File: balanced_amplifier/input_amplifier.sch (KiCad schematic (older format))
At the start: 47 parts, among them U1 LM4562, U2 LM4562, U3 NE5532, U4 LM4562

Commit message: specify resistor details
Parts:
- R1, R13, R16, R4: Distributor (none) -> Digikey; Distributor PN (none) -> YAG2320CT-ND; Manufacturer (none) -> Yageo; Manufacturer PN (none) -> RT0603FRE07100RL; URL (none) -> https://www.digikey.com/product-detail/en/yageo/RT0603FRE07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; Unit Price (none) -> 0.10
- R10, R11, R19, R20, R22, R23, R7, R8: Distributor (none) -> Digikey; Distributor PN (none) -> P820DBCT-ND; Manufacturer (none) -> Panasonic; Manufacturer PN (none) -> ERA-3AEB821V; URL (none) -> https://www.digikey.com/product-detail/en/panasonic-electro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; Unit Price (none) -> 0.35
- R12, R21, R24, R9: Distributor (none) -> Digikey; Distributor PN (none) -> P1.6KBCCT-ND; Manufacturer (none) -> Panasonic; Manufacturer PN (none) -> ERA-8AEB162V; URL (none) -> https://www.digikey.com/product-detail/en/panasonic-electro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; Unit Price (none) -> 0.66
- R14, R15, R17, R18, R2, R3, R5, R6: Distributor (none) -> Digikey; Distributor PN (none) -> 311-2103-1-ND; Manufacturer (none) -> Yageo; Manufacturer PN (none) -> AT0603DRD07100KL; URL (none) -> https://www.digikey.com/product-detail/en/yageo/AT0603DRD07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; Unit Price (none) -> 0.25

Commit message: Assign footprint to potentiometers
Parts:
- RV1: footprint (none) -> Potentiometer_THT_custom:Potentiometer_Bourns_91_Dual_Horizontal
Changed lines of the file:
@@
 F 0 "RV1" H 8430 1246 50  0000 R CNN
 F 1 "5k" H 8430 1155 50  0000 R CNN
-F 2 "" H 8500 1200 50  0001 C CNN
+F 2 "Potentiometer_THT_custom:Potentiometer_Bourns_91_Dual_Horizontal" H 8500 1200 50  0001 C CNN
 F 3 "https://www.bourns.com/docs/Product-Datasheets/91_95.pdf" H 8500 1200 50  0001 C CNN
 F 4 "Bourns" H 8500 1200 50  0001 C CNN "Manufacturer"
@@
 F 0 "RV1" H 8431 4254 50  0000 R CNN
 F 1 "5k" H 8431 4345 50  0000 R CNN
-F 2 "" H 8500 4300 50  0001 C CNN
+F 2 "Potentiometer_THT_custom:Potentiometer_Bourns_91_Dual_Horizontal" H 8500 4300 50  0001 C CNN
 F 3 "https://www.bourns.com/docs/Product-Datasheets/91_95.pdf" H 8500 4300 50  0001 C CNN
 F 4 "Bourns" H 8500 4300 50  0001 C CNN "Manufacturer"

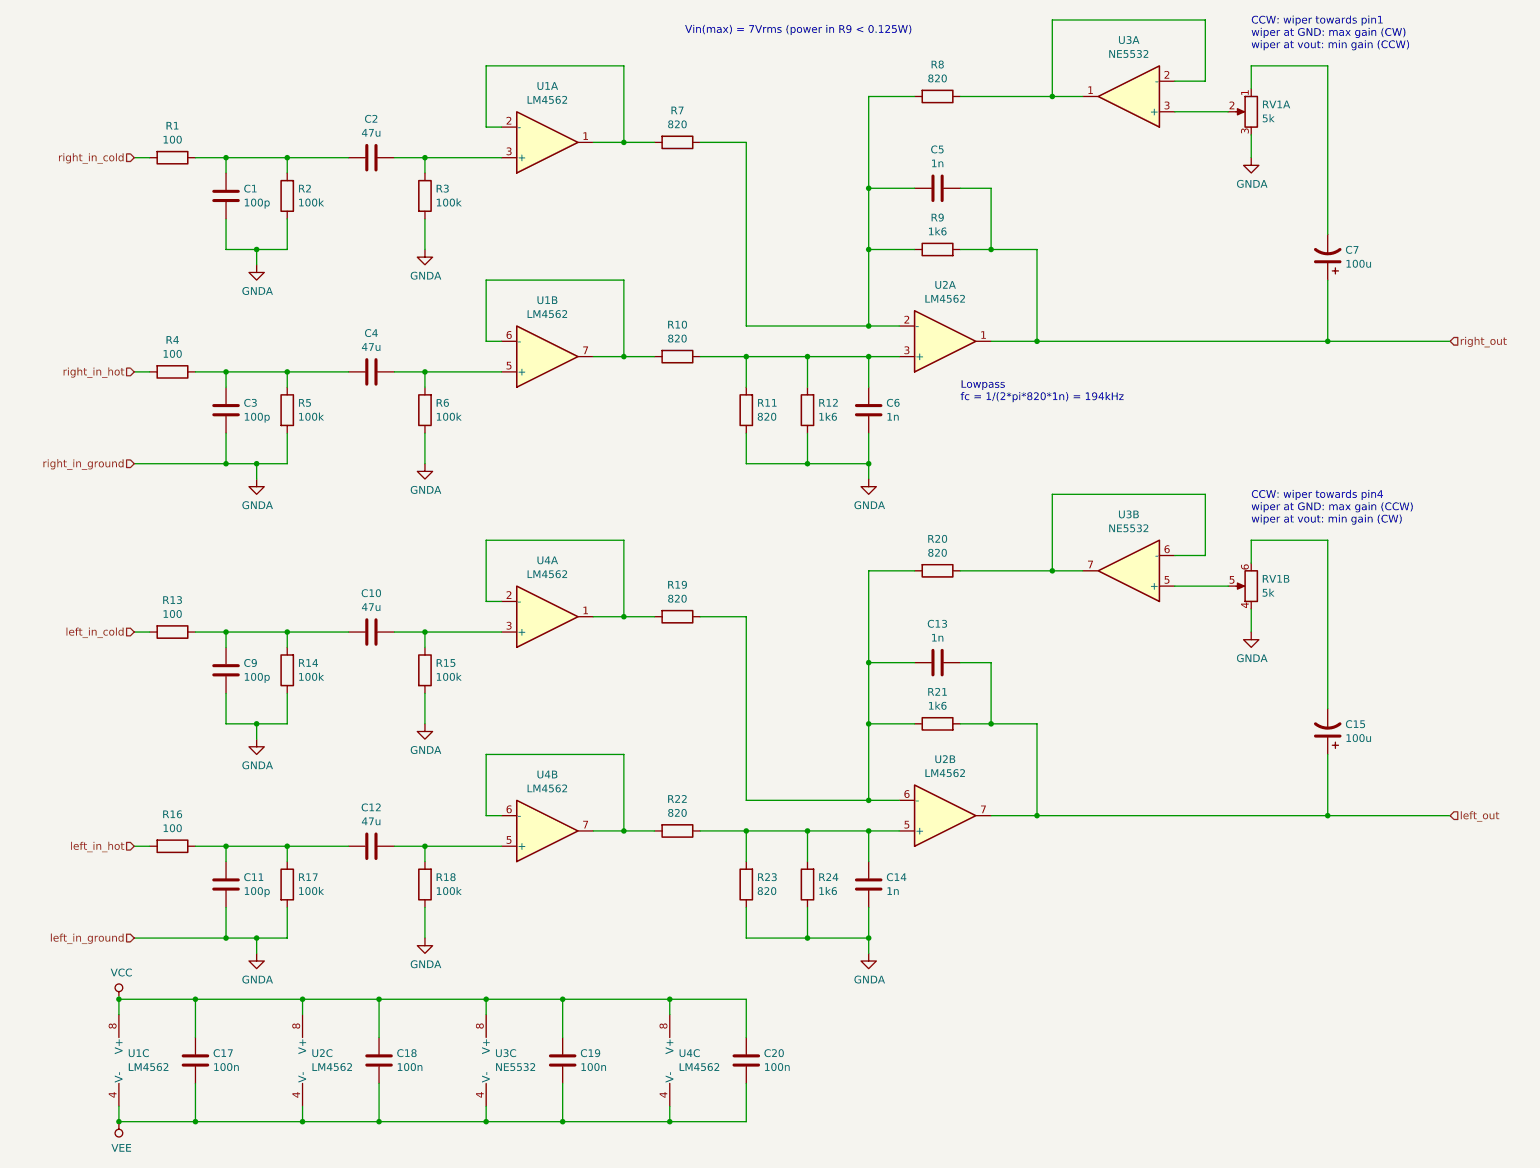
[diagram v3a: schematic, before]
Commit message: Add testpoints
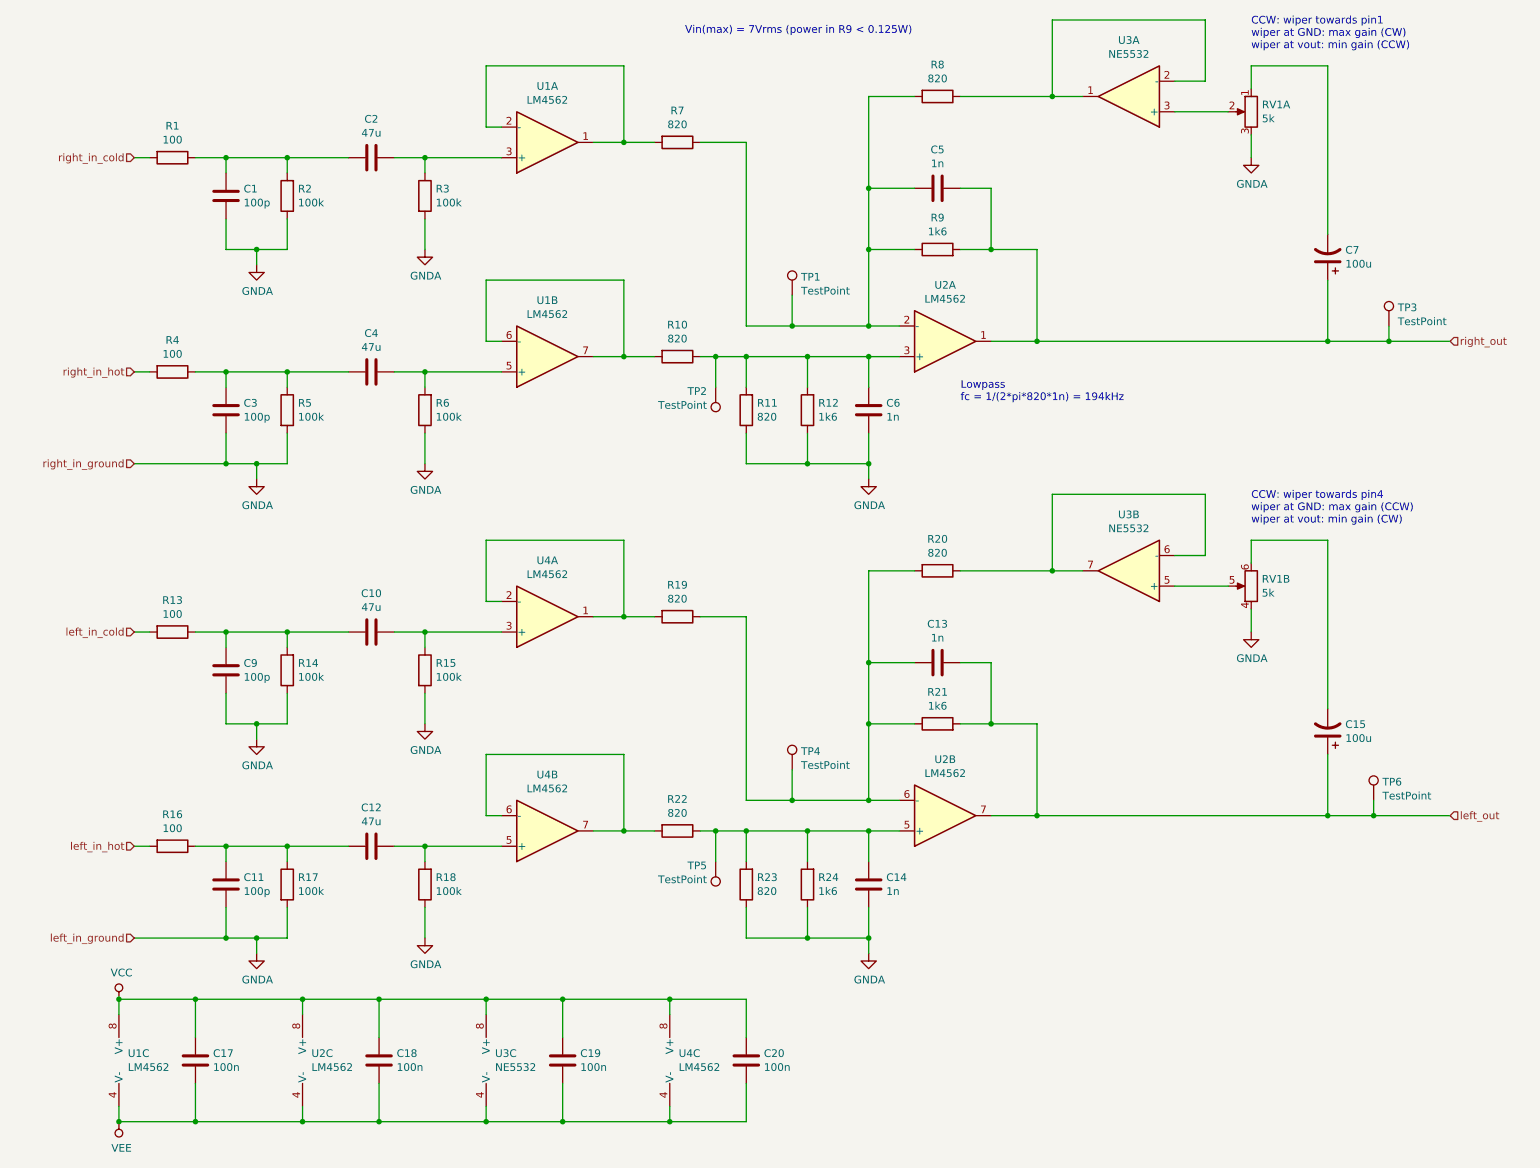
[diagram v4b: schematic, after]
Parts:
- added TP1, TP2, TP3, TP4, TP5, TP6: TestPoint, TestPoint:TestPoint_Keystone_5000-5004_Miniature, symbol Connector:TestPoint
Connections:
- net left_out: now also TP6.1
- net right_out: now also TP3.1
- net at C5.2, R7.1, R8.2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: now also TP1.1
- net at C6.1, R10.1, R11.2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: now also TP2.1
- net at C13.2, R19.1, R20.2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: now also TP4.1
- net at C14.1, R22.1, R23.2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: now also TP5.1
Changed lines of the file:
@@
 $EndComp
 Wire Wire Line
-	4900 2800 5200 2800
+	4900 2800 5000 2800
 Wire Wire Line
 	5600 3000 5600 2800
@@
 Connection ~ 6000 2100
 Wire Wire Line
-	6000 2600 5200 2600
+	6000 2600 5500 2600
 Connection ~ 6000 2600
 Connection ~ 6000 1700
@@
 $EndComp
 Wire Wire Line
-	4900 5900 5200 5900
+	4900 5900 5000 5900
 Wire Wire Line
 	5600 6100 5600 5900
@@
 Connection ~ 6000 5200
 Wire Wire Line
-	6000 5700 5200 5700
+	6000 5700 5500 5700
 Connection ~ 6000 5700
 Connection ~ 6000 4800
@@
 Vin(max) = 7Vrms (power in R9 < 0.125W)
 Wire Wire Line
-	9000 2700 9800 2700
-Wire Wire Line
-	9000 5800 9800 5800
+	9000 5800 9300 5800
+$Comp
+L Connector:TestPoint TP3
+U 1 1 5C15E7ED
+P 9400 2600
+F 0 "TP3" H 9458 2720 50  0000 L CNN
+F 1 "TestPoint" H 9458 2629 50  0000 L CNN
+F 2 "TestPoint:TestPoint_Keystone_5000-5004_Miniature" H 9600 2600 50  0001 C CNN
+F 3 "http://www.keyelco.com/product-pdf.cfm?p=1311" H 9600 2600 50  0001 C CNN
+F 4 "Keystone" H 9400 2600 50  0001 C CNN "Manufacturer"
+F 5 "5002" H 9400 2600 50  0001 C CNN "Manufacturer PN"
+F 6 "Digikey" H 9400 2600 50  0001 C CNN "Distributor"
+F 7 "36-5002-ND" H 9400 2600 50  0001 C CNN "Distributor PN"
+F 8 "https://www.digikey.com/products/en?keywords=36-5002-ND" H 9400 2600 50  0001 C CNN "URL"
+F 9 "0.37" H 9400 2600 50  0001 C CNN "Unit Price"
+	1    9400 2600
+	1    0    0    -1
+$EndComp
+$Comp
+L Connector:TestPoint TP6
+U 1 1 5C16979A
+P 9300 5700
+F 0 "TP6" H 9358 5820 50  0000 L CNN
+F 1 "TestPoint" H 9358 5729 50  0000 L CNN
+F 2 "TestPoint:TestPoint_Keystone_5000-5004_Miniature" H 9500 5700 50  0001 C CNN
+F 3 "http://www.keyelco.com/product-pdf.cfm?p=1311" H 9500 5700 50  0001 C CNN
+F 4 "Keystone" H 9300 5700 50  0001 C CNN "Manufacturer"
+F 5 "5002" H 9300 5700 50  0001 C CNN "Manufacturer PN"
+F 6 "Digikey" H 9300 5700 50  0001 C CNN "Distributor"
+F 7 "36-5002-ND" H 9300 5700 50  0001 C CNN "Distributor PN"
+F 8 "https://www.digikey.com/products/en?keywords=36-5002-ND" H 9300 5700 50  0001 C CNN "URL"
+F 9 "0.37" H 9300 5700 50  0001 C CNN "Unit Price"
+	1    9300 5700
+	1    0    0    -1
+$EndComp
+Wire Wire Line
+	9000 2700 9400 2700
+Wire Wire Line
+	9400 2600 9400 2700
+Connection ~ 9400 2700
+Wire Wire Line
+	9400 2700 9800 2700
+Wire Wire Line
+	9300 5700 9300 5800
+Connection ~ 9300 5800
+Wire Wire Line
+	9300 5800 9800 5800
+$Comp
+L Connector:TestPoint TP1
+U 1 1 5C17EF5C
+P 5500 2400
+F 0 "TP1" H 5558 2520 50  0000 L CNN
+F 1 "TestPoint" H 5558 2429 50  0000 L CNN
+F 2 "TestPoint:TestPoint_Keystone_5000-5004_Miniature" H 5700 2400 50  0001 C CNN
+F 3 "http://www.keyelco.com/product-pdf.cfm?p=1311" H 5700 2400 50  0001 C CNN
+F 4 "Keystone" H 5500 2400 50  0001 C CNN "Manufacturer"
+F 5 "5002" H 5500 2400 50  0001 C CNN "Manufacturer PN"
+F 6 "Digikey" H 5500 2400 50  0001 C CNN "Distributor"
+F 7 "36-5002-ND" H 5500 2400 50  0001 C CNN "Distributor PN"
+F 8 "https://www.digikey.com/products/en?keywords=36-5002-ND" H 5500 2400 50  0001 C CNN "URL"
+F 9 "0.37" H 5500 2400 50  0001 C CNN "Unit Price"
+	1    5500 2400
+	1    0    0    -1
+$EndComp
+$Comp
+L Connector:TestPoint TP4
+U 1 1 5C17F1EE
+P 5500 5500
+F 0 "TP4" H 5558 5620 50  0000 L CNN
+F 1 "TestPoint" H 5558 5529 50  0000 L CNN
+F 2 "TestPoint:TestPoint_Keystone_5000-5004_Miniature" H 5700 5500 50  0001 C CNN
+F 3 "http://www.keyelco.com/product-pdf.cfm?p=1311" H 5700 5500 50  0001 C CNN
+F 4 "Keystone" H 5500 5500 50  0001 C CNN "Manufacturer"
+F 5 "5002" H 5500 5500 50  0001 C CNN "Manufacturer PN"
+F 6 "Digikey" H 5500 5500 50  0001 C CNN "Distributor"
+F 7 "36-5002-ND" H 5500 5500 50  0001 C CNN "Distributor PN"
+F 8 "https://www.digikey.com/products/en?keywords=36-5002-ND" H 5500 5500 50  0001 C CNN "URL"
+F 9 "0.37" H 5500 5500 50  0001 C CNN "Unit Price"
+	1    5500 5500
+	1    0    0    -1
+$EndComp
+$Comp
+L Connector:TestPoint TP2
+U 1 1 5C17F304
+P 5000 3000
+F 0 "TP2" H 4943 3027 50  0000 R CNN
+F 1 "TestPoint" H 4943 3118 50  0000 R CNN
+F 2 "TestPoint:TestPoint_Keystone_5000-5004_Miniature" H 5200 3000 50  0001 C CNN
+F 3 "http://www.keyelco.com/product-pdf.cfm?p=1311" H 5200 3000 50  0001 C CNN
+F 4 "Keystone" H 5000 3000 50  0001 C CNN "Manufacturer"
+F 5 "5002" H 5000 3000 50  0001 C CNN "Manufacturer PN"
+F 6 "Digikey" H 5000 3000 50  0001 C CNN "Distributor"
+F 7 "36-5002-ND" H 5000 3000 50  0001 C CNN "Distributor PN"
+F 8 "https://www.digikey.com/products/en?keywords=36-5002-ND" H 5000 3000 50  0001 C CNN "URL"
+F 9 "0.37" H 5000 3000 50  0001 C CNN "Unit Price"
+	1    5000 3000
+	1    0    0    1
+$EndComp
+$Comp
+L Connector:TestPoint TP5
+U 1 1 5C17F5A2
+P 5000 6100
+F 0 "TP5" H 4943 6127 50  0000 R CNN
+F 1 "TestPoint" H 4943 6218 50  0000 R CNN
+F 2 "TestPoint:TestPoint_Keystone_5000-5004_Miniature" H 5200 6100 50  0001 C CNN
+F 3 "http://www.keyelco.com/product-pdf.cfm?p=1311" H 5200 6100 50  0001 C CNN
+F 4 "Keystone" H 5000 6100 50  0001 C CNN "Manufacturer"
+F 5 "5002" H 5000 6100 50  0001 C CNN "Manufacturer PN"
+F 6 "Digikey" H 5000 6100 50  0001 C CNN "Distributor"
+F 7 "36-5002-ND" H 5000 6100 50  0001 C CNN "Distributor PN"
+F 8 "https://www.digikey.com/products/en?keywords=36-5002-ND" H 5000 6100 50  0001 C CNN "URL"
+F 9 "0.37" H 5000 6100 50  0001 C CNN "Unit Price"
+	1    5000 6100
+	1    0    0    1
+$EndComp
+Wire Wire Line
+	5000 6100 5000 5900
+Connection ~ 5000 5900
+Wire Wire Line
+	5000 5900 5200 5900
+Wire Wire Line
+	5000 3000 5000 2800
+Connection ~ 5000 2800
+Wire Wire Line
+	5000 2800 5200 2800
+Wire Wire Line
+	5500 2400 5500 2600
+Connection ~ 5500 2600
+Wire Wire Line
+	5500 2600 5200 2600
+Wire Wire Line
+	5500 5500 5500 5700
+Connection ~ 5500 5700
+Wire Wire Line
+	5500 5700 5200 5700
 $EndSCHEMATC
